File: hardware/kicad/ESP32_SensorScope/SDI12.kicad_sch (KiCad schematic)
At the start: 20 parts, among them J5 Conn_01x01_Socket, J6 Conn_01x01_Socket, U6 SN74LV1T125DBV, U7 74LVC1G240DBVRG4, U8 74LVC1G240DBVRG4

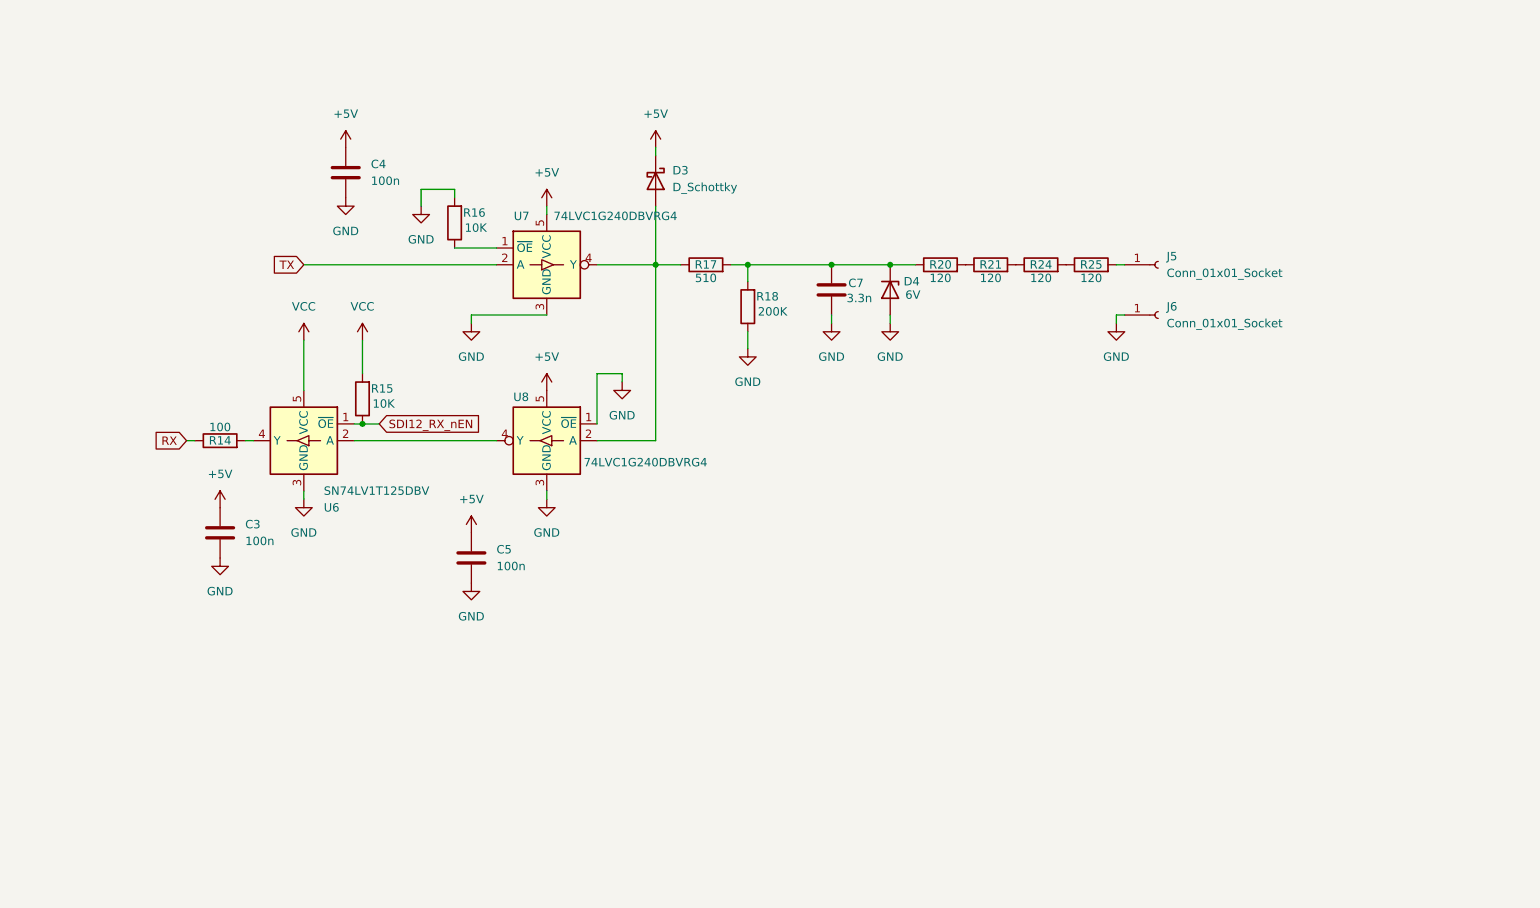
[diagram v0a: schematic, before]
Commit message: som updates on the schematics
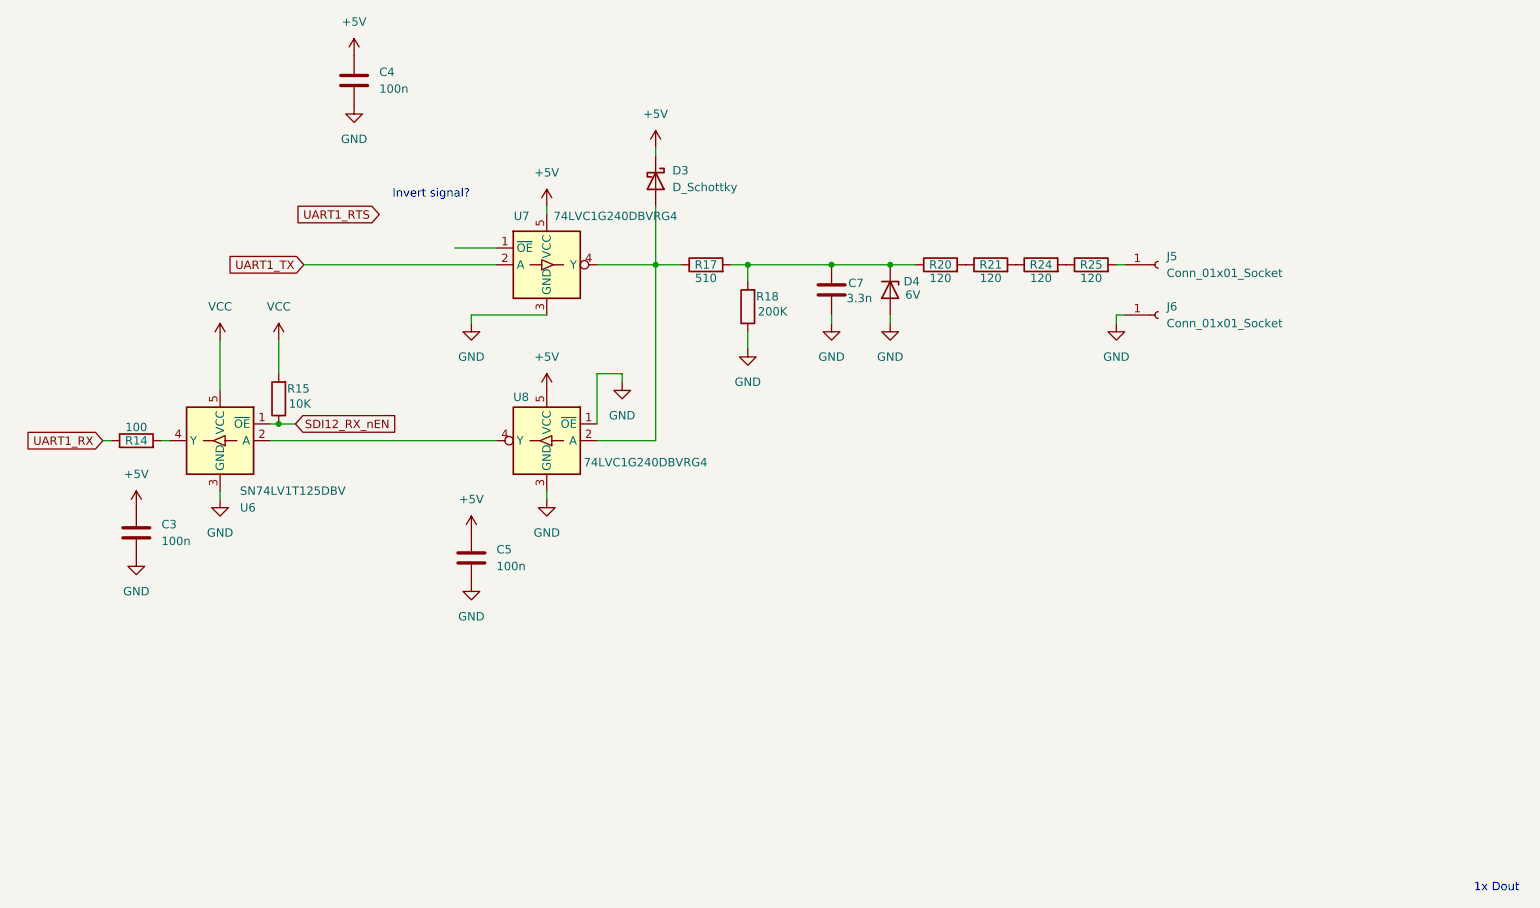
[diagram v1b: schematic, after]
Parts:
- removed R16: 10K, symbol Device:R
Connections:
- net RX renamed UART1_RX
- net TX renamed UART1_TX
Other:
- note added: "1x Dout"
- note added: "Invert signal?"
- moved on the sheet: C3, C4, R14, R15, U6
